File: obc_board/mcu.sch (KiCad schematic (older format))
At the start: 41 parts, among them J8 Conn_01x08_Female, J9 Micro_SD_Card, U3 STM32L552ZE, Y1 32.768kHz, Y2 8MHz

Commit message: layout done
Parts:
- removed R12, R13, R14, R15, R16, R17: 100k, Resistor_SMD:R_0402_1005Metric, symbol Device:R
- renumbered C9 to C10, C10 to C11, C11 to C12, C12 to C13, C13 to C8, C8 to C9, J8 to J4, J9 to J5, R18 to R12, R19 to R13, R20 to R14, R21 to R15
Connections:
- wire segments 190 -> 166
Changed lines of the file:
@@
 	5100 5250 5450 5250
 $Comp
-L Device:C C8
+L Device:C C9
 U 1 1 5E7F4400
 P 5450 5000
-F 0 "C8" H 5565 5046 50  0000 L CNN
+F 0 "C9" H 5565 5046 50  0000 L CNN
 F 1 "100n" H 5565 4955 50  0000 L CNN
 F 2 "Capacitor_SMD:C_0402_1005Metric" H 5488 4850 50  0001 C CNN
@@
 $EndComp
 $Comp
-L Device:C C10
+L Device:C C11
 U 1 1 5E8976B8
 P 5700 6100
-F 0 "C10" V 5952 6100 50  0000 C CNN
+F 0 "C11" V 5952 6100 50  0000 C CNN
 F 1 "20p" V 5861 6100 50  0000 C CNN
 F 2 "Capacitor_SMD:C_0201_0603Metric" H 5738 5950 50  0001 C CNN
@@
 $EndComp
 $Comp
-L Device:C C9
+L Device:C C10
 U 1 1 5E8976BE
 P 5700 5600
-F 0 "C9" V 5952 5600 50  0000 C CNN
+F 0 "C10" V 5952 5600 50  0000 C CNN
 F 1 "20p" V 5861 5600 50  0000 C CNN
 F 2 "Capacitor_SMD:C_0201_0603Metric" H 5738 5450 50  0001 C CNN
@@
 	6150 750  6150 650
 $Comp
-L Device:C C11
+L Device:C C12
 U 1 1 5E85C7EE
 P 6150 900
-F 0 "C11" V 5898 900 50  0000 C CNN
+F 0 "C12" V 5898 900 50  0000 C CNN
 F 1 "100n" V 5989 900 50  0000 C CNN
 F 2 "Capacitor_SMD:C_0402_1005Metric" H 6188 750 50  0001 C CNN
@@
 GND
 $Comp
-L Device:C C12
+L Device:C C13
 U 1 1 5E7FDC18
 P 6550 900
-F 0 "C12" V 6298 900 50  0000 C CNN
+F 0 "C13" V 6298 900 50  0000 C CNN
 F 1 "100n" V 6389 900 50  0000 C CNN
 F 2 "Capacitor_SMD:C_0402_1005Metric" H 6588 750 50  0001 C CNN
@@
 I2C2_SCL
 $Comp
-L Device:R R18
+L Device:R R12
 U 1 1 5F6F5F72
 P 9450 6000
-F 0 "R18" H 9520 6046 50  0000 L CNN
+F 0 "R12" H 9520 6046 50  0000 L CNN
 F 1 "10k" H 9520 5955 50  0000 L CNN
 F 2 "Resistor_SMD:R_0402_1005Metric" V 9380 6000 50  0001 C CNN
@@
 	4550 7000 5200 7000
 $Comp
-L Device:R R19
+L Device:R R13
 U 1 1 5F9FC147
 P 9800 6000
-F 0 "R19" H 9870 6046 50  0000 L CNN
+F 0 "R13" H 9870 6046 50  0000 L CNN
 F 1 "10k" H 9870 5955 50  0000 L CNN
 F 2 "Resistor_SMD:R_0402_1005Metric" V 9730 6000 50  0001 C CNN
@@
 $EndComp
 $Comp
-L Device:R R20
+L Device:R R14
 U 1 1 5FA039E4
 P 10150 6000
-F 0 "R20" H 10220 6046 50  0000 L CNN
+F 0 "R14" H 10220 6046 50  0000 L CNN
 F 1 "10k" H 10220 5955 50  0000 L CNN
 F 2 "Resistor_SMD:R_0402_1005Metric" V 10080 6000 50  0001 C CNN
@@
 $EndComp
 $Comp
-L Device:R R21
+L Device:R R15
 U 1 1 5FA0B331
 P 10500 6000
-F 0 "R21" H 10570 6046 50  0000 L CNN
+F 0 "R15" H 10570 6046 50  0000 L CNN
 F 1 "10k" H 10570 5955 50  0000 L CNN
 F 2 "Resistor_SMD:R_0402_1005Metric" V 10430 6000 50  0001 C CNN
@@
 $EndComp
 $Comp
-L Device:C C13
+L Device:C C8
 U 1 1 5FA12D6C
 P 5200 7200
-F 0 "C13" H 5315 7246 50  0000 L CNN
+F 0 "C8" H 5315 7246 50  0000 L CNN
 F 1 "100n" H 5315 7155 50  0000 L CNN
 F 2 "Capacitor_SMD:C_0402_1005Metric" H 5238 7050 50  0001 C CNN
@@
 Connection ~ 5450 4800
 $Comp
-L Connector:Micro_SD_Card J9
+L Connector:Micro_SD_Card J5
 U 1 1 5F37C195
 P 3650 7000
-F 0 "J9" H 3600 6183 50  0000 C CNN
+F 0 "J5" H 3600 6183 50  0000 C CNN
 F 1 "Micro_SD_Card" H 3600 6274 50  0000 C CNN
 F 2 "cubesat_obc:microSD_HC_Wuerth_693072010801" H 4800 7300 50  0001 C CNN
@@
 GND
 $Comp
-L Connector:Conn_01x08_Female J8
+L Connector:Conn_01x08_Female J4
 U 1 1 5F3C5B25
 P 1600 6900
-F 0 "J8" H 1492 6275 50  0000 C CNN
+F 0 "J4" H 1492 6275 50  0000 C CNN
 F 1 "Conn_01x08_Female" H 1492 6366 50  0000 C CNN
 F 2 "Connector_Molex:Molex_PicoBlade_53261-0871_1x08-1MP_P1.25mm_Horizontal" H 1600 6900 50  0001 C CNN
@@
 Text HLabel 2400 4300 3    50   Input ~ 0
 PG5
-Wire Wire Line
-	7950 5800 7950 6250
-Wire Wire Line
-	7250 6450 7000 6450
-Wire Wire Line
-	7250 5800 7250 6450
-Wire Wire Line
-	7600 6350 7000 6350
-Wire Wire Line
-	7600 5800 7600 6350
-Wire Wire Line
-	7950 6250 7000 6250
-Wire Wire Line
-	8300 6150 7000 6150
-Wire Wire Line
-	8300 5800 8300 6150
-Wire Wire Line
-	8650 6050 7000 6050
-Wire Wire Line
-	8650 5800 8650 6050
-Wire Wire Line
-	9000 5950 7000 5950
-Wire Wire Line
-	9000 5800 9000 5950
-Wire Wire Line
-	9000 5400 9000 5500
-Wire Wire Line
-	8650 5400 9000 5400
-Wire Wire Line
-	8650 5400 8650 5500
-Connection ~ 8650 5400
-Wire Wire Line
-	8300 5400 8650 5400
-$Comp
-L Device:R R17
-U 1 1 5F5A60A6
-P 9000 5650
-F 0 "R17" H 9070 5696 50  0000 L CNN
-F 1 "100k" H 9070 5605 50  0000 L CNN
-F 2 "Resistor_SMD:R_0402_1005Metric" V 8930 5650 50  0001 C CNN
-F 3 "https://www.yageo.com/upload/media/product/productsearch/datasheet/rchip/PYu-RC_Group_51_RoHS_L_11.pdf" H 9000 5650 50  0001 C CNN
-F 4 "311-100KLRCT-ND" H 9000 5650 50  0001 C CNN "Digikey Part Number"
-	1    9000 5650
-	1    0    0    -1
-$EndComp
-$Comp
-L Device:R R16
-U 1 1 5F5A60A0
-P 8650 5650
-F 0 "R16" H 8720 5696 50  0000 L CNN
-F 1 "100k" H 8720 5605 50  0000 L CNN
-F 2 "Resistor_SMD:R_0402_1005Metric" V 8580 5650 50  0001 C CNN
-F 3 "https://www.yageo.com/upload/media/product/productsearch/datasheet/rchip/PYu-RC_Group_51_RoHS_L_11.pdf" H 8650 5650 50  0001 C CNN
-F 4 "311-100KLRCT-ND" H 8650 5650 50  0001 C CNN "Digikey Part Number"
-	1    8650 5650
-	1    0    0    -1
-$EndComp
-Text HLabel 7000 6450 0    50   Input ~ 0
-USART3_TX
-Text HLabel 7000 6350 0    50   Input ~ 0
-USART3_RX
-Wire Wire Line
-	8300 5400 8300 5500
-Connection ~ 8300 5400
-Wire Wire Line
-	7950 5400 8300 5400
-$Comp
-L Device:R R15
-U 1 1 5F4D928A
-P 8300 5650
-F 0 "R15" H 8370 5696 50  0000 L CNN
-F 1 "100k" H 8370 5605 50  0000 L CNN
-F 2 "Resistor_SMD:R_0402_1005Metric" V 8230 5650 50  0001 C CNN
-F 3 "https://www.yageo.com/upload/media/product/productsearch/datasheet/rchip/PYu-RC_Group_51_RoHS_L_11.pdf" H 8300 5650 50  0001 C CNN
-F 4 "311-100KLRCT-ND" H 8300 5650 50  0001 C CNN "Digikey Part Number"
-	1    8300 5650
-	1    0    0    -1
-$EndComp
-Wire Wire Line
-	7950 5400 7950 5500
-Connection ~ 7950 5400
-Wire Wire Line
-	7600 5400 7950 5400
-$Comp
-L Device:R R14
-U 1 1 5F4B9F38
-P 7950 5650
-F 0 "R14" H 8020 5696 50  0000 L CNN
-F 1 "100k" H 8020 5605 50  0000 L CNN
-F 2 "Resistor_SMD:R_0402_1005Metric" V 7880 5650 50  0001 C CNN
-F 3 "https://www.yageo.com/upload/media/product/productsearch/datasheet/rchip/PYu-RC_Group_51_RoHS_L_11.pdf" H 7950 5650 50  0001 C CNN
-F 4 "311-100KLRCT-ND" H 7950 5650 50  0001 C CNN "Digikey Part Number"
-	1    7950 5650
-	1    0    0    -1
-$EndComp
-Wire Wire Line
-	7600 5400 7600 5500
-Connection ~ 7600 5400
-Wire Wire Line
-	7250 5400 7600 5400
-$Comp
-L Device:R R13
-U 1 1 5F49BE24
-P 7600 5650
-F 0 "R13" H 7670 5696 50  0000 L CNN
-F 1 "100k" H 7670 5605 50  0000 L CNN
-F 2 "Resistor_SMD:R_0402_1005Metric" V 7530 5650 50  0001 C CNN
-F 3 "https://www.yageo.com/upload/media/product/productsearch/datasheet/rchip/PYu-RC_Group_51_RoHS_L_11.pdf" H 7600 5650 50  0001 C CNN
-F 4 "311-100KLRCT-ND" H 7600 5650 50  0001 C CNN "Digikey Part Number"
-	1    7600 5650
-	1    0    0    -1
-$EndComp
-Wire Wire Line
-	7250 5400 7250 5500
-Connection ~ 7250 5400
-Wire Wire Line
-	7000 5400 7250 5400
-$Comp
-L Device:R R12
-U 1 1 5F47EB27
-P 7250 5650
-F 0 "R12" H 7320 5696 50  0000 L CNN
-F 1 "100k" H 7320 5605 50  0000 L CNN
-F 2 "Resistor_SMD:R_0402_1005Metric" V 7180 5650 50  0001 C CNN
-F 3 "https://www.yageo.com/upload/media/product/productsearch/datasheet/rchip/PYu-RC_Group_51_RoHS_L_11.pdf" H 7250 5650 50  0001 C CNN
-F 4 "311-100KLRCT-ND" H 7250 5650 50  0001 C CNN "Digikey Part Number"
-	1    7250 5650
-	1    0    0    -1
-$EndComp
-Text HLabel 7000 5400 0    50   Input ~ 0
-3V3
-Text HLabel 7000 6250 0    50   Input ~ 0
-USART2_TX
-Text HLabel 7000 6150 0    50   Input ~ 0
-USART2_RX
-Text HLabel 7000 5950 0    50   Input ~ 0
-USART1_RX
-Text HLabel 7000 6050 0    50   Input ~ 0
-USART1_TX
 Text HLabel 8700 5150 3    50   Input ~ 0
 GND

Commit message: relayout
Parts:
- removed C12, C13, C14, C15, C21, C22, C23, C24, C3, C4, C5, C9: 100n, Capacitor_SMD:C_0402_1005Metric, symbol Device:C
- removed C19: 1u, Capacitor_SMD:CP_Elec_4x5.3, symbol Device:CP
- removed C20, C25: 4.7u, Capacitor_SMD:CP_Elec_4x5.3, symbol Device:CP
- removed R11: 100k, Resistor_SMD:R_0402_1005Metric, symbol Device:R
- removed U3: STM32L552ZE, cubesat_obc:LQFP-144_20x20mm_P0.5mm, symbol cubesat_obc_lib:STM32L552ZET6
- added C51: 1u, Capacitor_SMD:C_0603_1608Metric, symbol Device:CP
- added C52, C54, C57, C58, C60, C62, C64, C66, C67, C68, C69, C71, C73: 100n, Capacitor_SMD:C_0402_1005Metric, symbol Device:C
- added C53, C55: 4.7u, Capacitor_SMD:C_0805_2012Metric, symbol Device:CP
- added C74: 4.7u, Capacitor_SMD:C_0201_0603Metric, symbol Device:C
- added L10: 4.7u, cubesat_obc:L_Vishay_IHLP-2020, symbol Device:L
- added R21, R24: 10k, Resistor_SMD:R_0402_1005Metric, symbol Device:R
- added U19: STM32L552ZET6Q, Package_QFP:LQFP-144_20x20mm_P0.5mm, symbol cubesat_obc_lib:STM32L552ZET6Q
- C65: renamed from C18; footprint Capacitor_SMD:CP_Elec_4x5.3 -> Capacitor_SMD:C_0603_1608Metric; Digikey Part Number 565-2486-1-ND -> 311-1446-2-ND
- renumbered C10 to C56, C11 to C59, C16 to C61, C17 to C63, C7 to C70, C6 to C72, C8 to C75, J4 to J16, J5 to J17, R12 to R115, R13 to R116, R14 to R117, R15 to R118, R9 to R119, R10 to R120, Y2 to Y3, Y1 to Y4
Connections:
- net labels added: I2C4_SCL, I2C4_SDA, NJTRST, PA10, PA11, PA12, PC6, PC7, PD0, PD1, PD10, PD11, PD12, PD13, PD14, PD15, PD5, PD7, PD8, PD9, PE10, PE7, PE8, PE9, PF10, PF11, PF12, PF13, PF9, PG12, PG15
- net labels removed: I2C3_SCL, I2C3_SDA, NJRST, OSC_IN, OSC_OUT, SPI3_MISO, SPI3_MOSI, SPI3_SCK
- wire segments 166 -> 205
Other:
- moved on the sheet: C56, C59, C61, C63, C65, C70, C72, C75, J16, J17, R115, R116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

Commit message: modify planes
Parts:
- renumbered J16 to JTAG1
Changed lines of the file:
@@
 $Descr A4 11693 8268
 encoding utf-8
-Sheet 8 8
+Sheet 8 9
 Title ""
 Date ""
@@
 Text HLabel 9500 3450 3    50   Input ~ 0
 GND
-$Comp
-L Connector:Conn_01x08_Female J16
-U 1 1 5F3C5B25
-P 6750 1600
-F 0 "J16" H 6642 975 50  0000 C CNN
-F 1 "Conn_01x08_Female" H 6642 1066 50  0000 C CNN
-F 2 "Connector_Molex:Molex_PicoBlade_53261-0871_1x08-1MP_P1.25mm_Horizontal" H 6750 1600 50  0001 C CNN
-F 3 "https://www.molex.com/pdm_docs/sd/532610871_sd.pdf" H 6750 1600 50  0001 C CNN
-F 4 "WM7626CT-ND" H 6750 1600 50  0001 C CNN "Digikey Part Number"
-	1    6750 1600
-	-1   0    0    1
-$EndComp
 Text HLabel 6950 1900 2    50   Input ~ 0
 GND
@@
 Text HLabel 4800 2650 1    50   Input ~ 0
 PC6
+$Comp
+L Connector:Conn_01x08_Female JTAG1
+U 1 1 5F3C5B25
+P 6750 1600
+F 0 "JTAG1" H 6642 975 50  0000 C CNN
+F 1 "Conn_01x08_Female" H 6642 1066 50  0000 C CNN
+F 2 "Connector_Molex:Molex_PicoBlade_53261-0871_1x08-1MP_P1.25mm_Horizontal" H 6750 1600 50  0001 C CNN
+F 3 "https://www.molex.com/pdm_docs/sd/532610871_sd.pdf" H 6750 1600 50  0001 C CNN
+F 4 "WM7626CT-ND" H 6750 1600 50  0001 C CNN "Digikey Part Number"
+	1    6750 1600
+	-1   0    0    1
+$EndComp
 $EndSCHEMATC

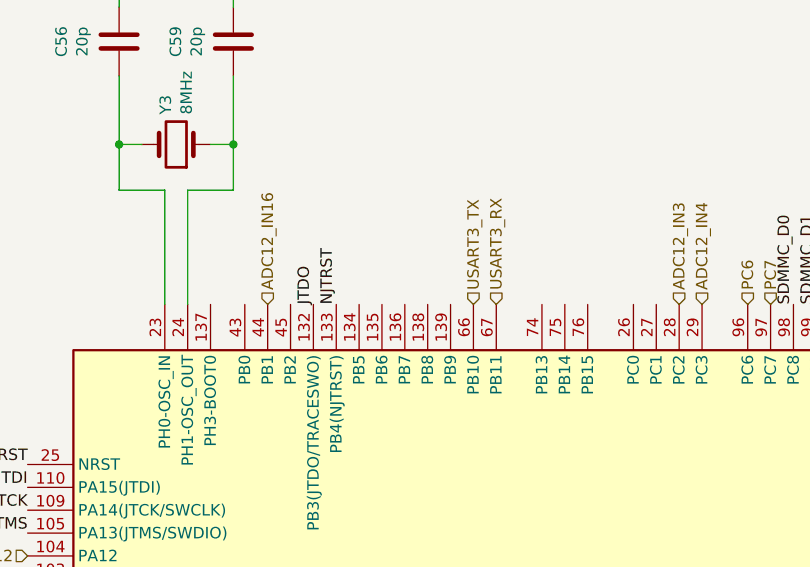
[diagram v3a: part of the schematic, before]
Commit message: added h bridge and magnetometers
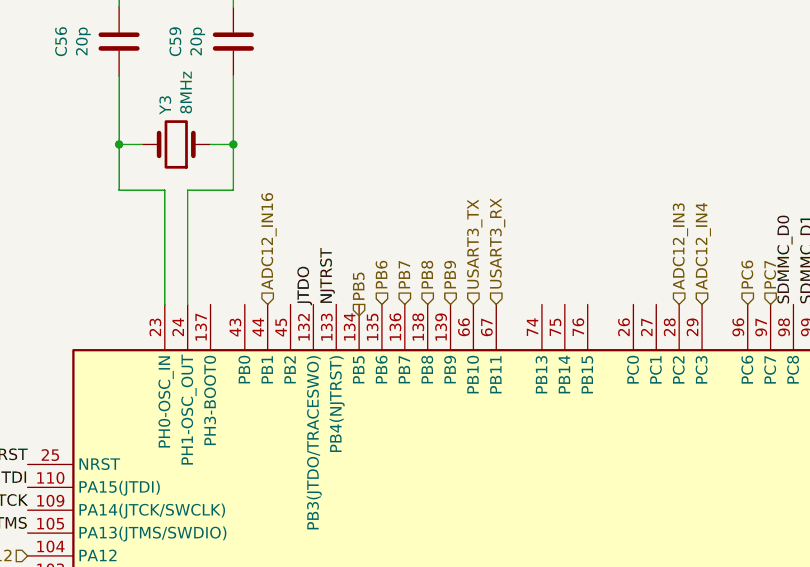
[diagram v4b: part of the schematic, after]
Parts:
- R119, R120: Digikey Part Number 311-100KLRCT-ND -> YAG2307CT-ND
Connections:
- net PB6: now reaches U19.135 (PB6)
- net PB7: now reaches U19.136 (PB7)
- net PB8: now reaches U19.138 (PB8)
- net PB9: now reaches U19.139 (PB9)
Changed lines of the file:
@@
 $Descr A4 11693 8268
 encoding utf-8
-Sheet 8 9
+Sheet 10 10
 Title ""
 Date ""
@@
 F 1 "100k" H 10470 3905 50  0000 L CNN
 F 2 "Resistor_SMD:R_0402_1005Metric" V 10330 3950 50  0001 C CNN
-F 3 "https://www.yageo.com/upload/media/product/productsearch/datasheet/rchip/PYu-RC_Group_51_RoHS_L_11.pdf" H 10400 3950 50  0001 C CNN
-F 4 "311-100KLRCT-ND" H 10400 3950 50  0001 C CNN "Digikey Part Number"
+F 3 "https://www.yageo.com/upload/media/product/productsearch/datasheet/rchip/PYu-RC_Group_51_RoHS_L_11.pdfhttps://www.yageo.com/upload/media/product/productsearch/datasheet/rchip/PYu-RT_1-to-0.01_RoHS_L_12.pdf" H 10400 3950 50  0001 C CNN
+F 4 "YAG2307CT-ND" H 10400 3950 50  0001 C CNN "Digikey Part Number"
 	1    10400 3950
 	1    0    0    -1
@@
 F 1 "100k" H 10470 4655 50  0000 L CNN
 F 2 "Resistor_SMD:R_0402_1005Metric" V 10330 4700 50  0001 C CNN
-F 3 "https://www.yageo.com/upload/media/product/productsearch/datasheet/rchip/PYu-RC_Group_51_RoHS_L_11.pdf" H 10400 4700 50  0001 C CNN
-F 4 "311-100KLRCT-ND" H 10400 4700 50  0001 C CNN "Digikey Part Number"
+F 3 "https://www.yageo.com/upload/media/product/productsearch/datasheet/rchip/PYu-RC_Group_51_RoHS_L_11.pdfhttps://www.yageo.com/upload/media/product/productsearch/datasheet/rchip/PYu-RT_1-to-0.01_RoHS_L_12.pdf" H 10400 4700 50  0001 C CNN
+F 4 "YAG2307CT-ND" H 10400 4700 50  0001 C CNN "Digikey Part Number"
 	1    10400 4700
 	1    0    0    -1
@@
 	-1   0    0    1
 $EndComp
+Text HLabel 3500 2650 1    50   Input ~ 0
+PB9
+Text HLabel 3400 2650 1    50   Input ~ 0
+PB8
+Text HLabel 3300 2650 1    50   Input ~ 0
+PB7
+Text HLabel 3200 2650 1    50   Input ~ 0
+PB6
+Text HLabel 3100 2700 1    50   Input ~ 0
+PB5
 $EndSCHEMATC
